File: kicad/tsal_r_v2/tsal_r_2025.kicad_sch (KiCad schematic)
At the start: 46 parts, among them J1 Conn_01x02_Pin, J2 Conn_01x02_Pin, U1 TL431LP, U2 LTV-817, U3 B1212, U4 2N7002, U5 2N7002, U6 NCE60P04R

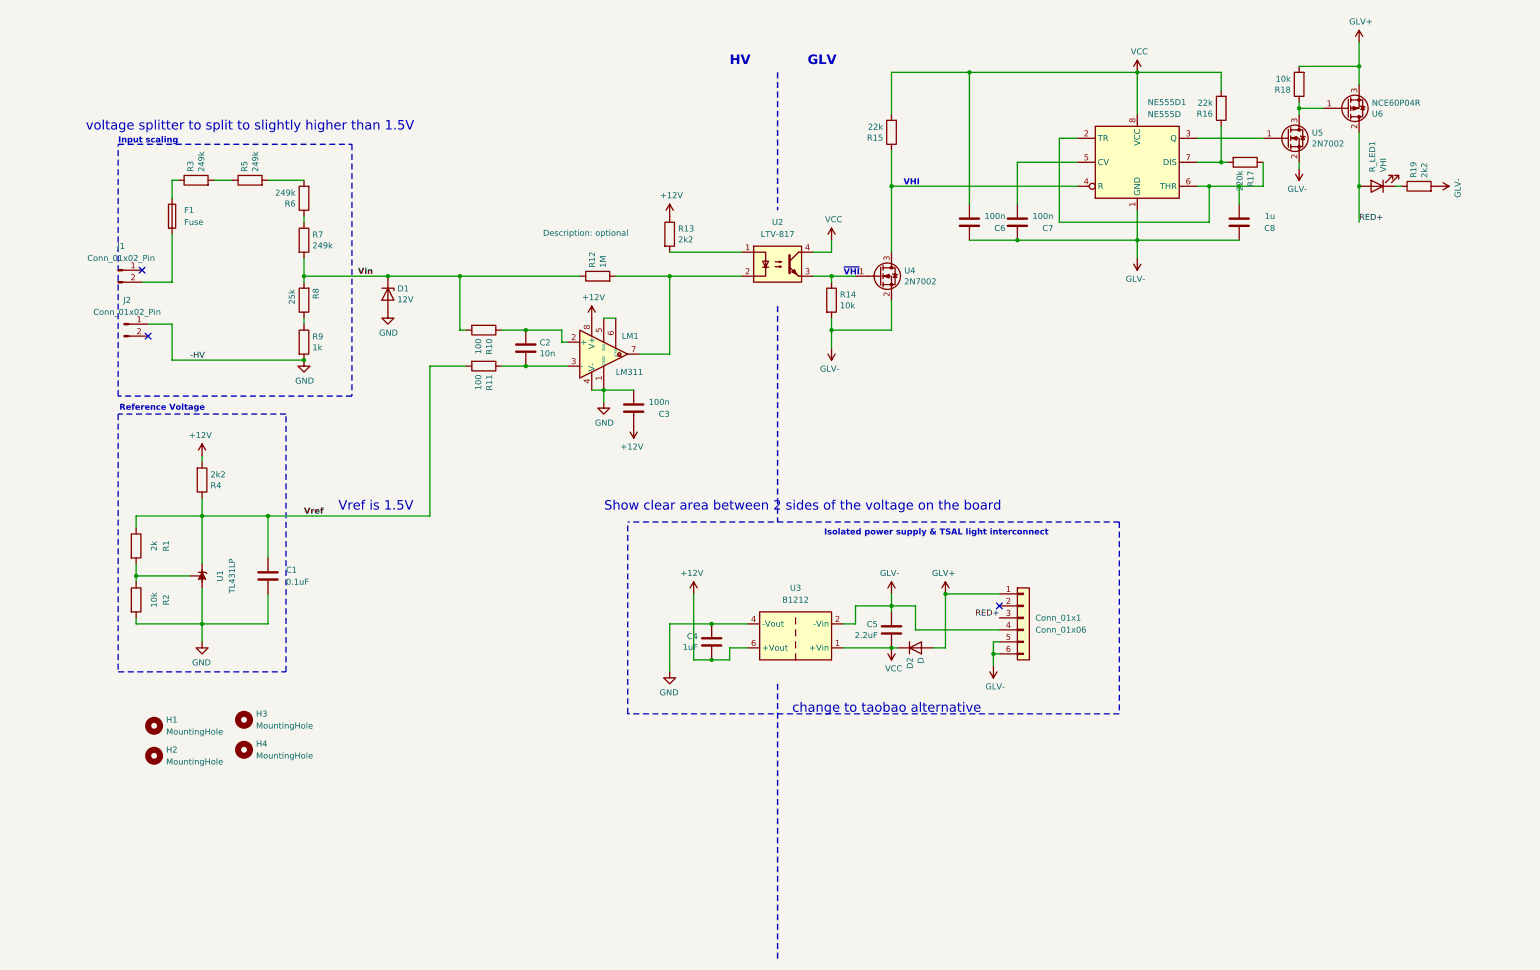
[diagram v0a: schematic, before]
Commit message: TSAL-R v3.0
Redesigned the TSAL-R, currently v3. with naming RBR-TSAL-R v3.0
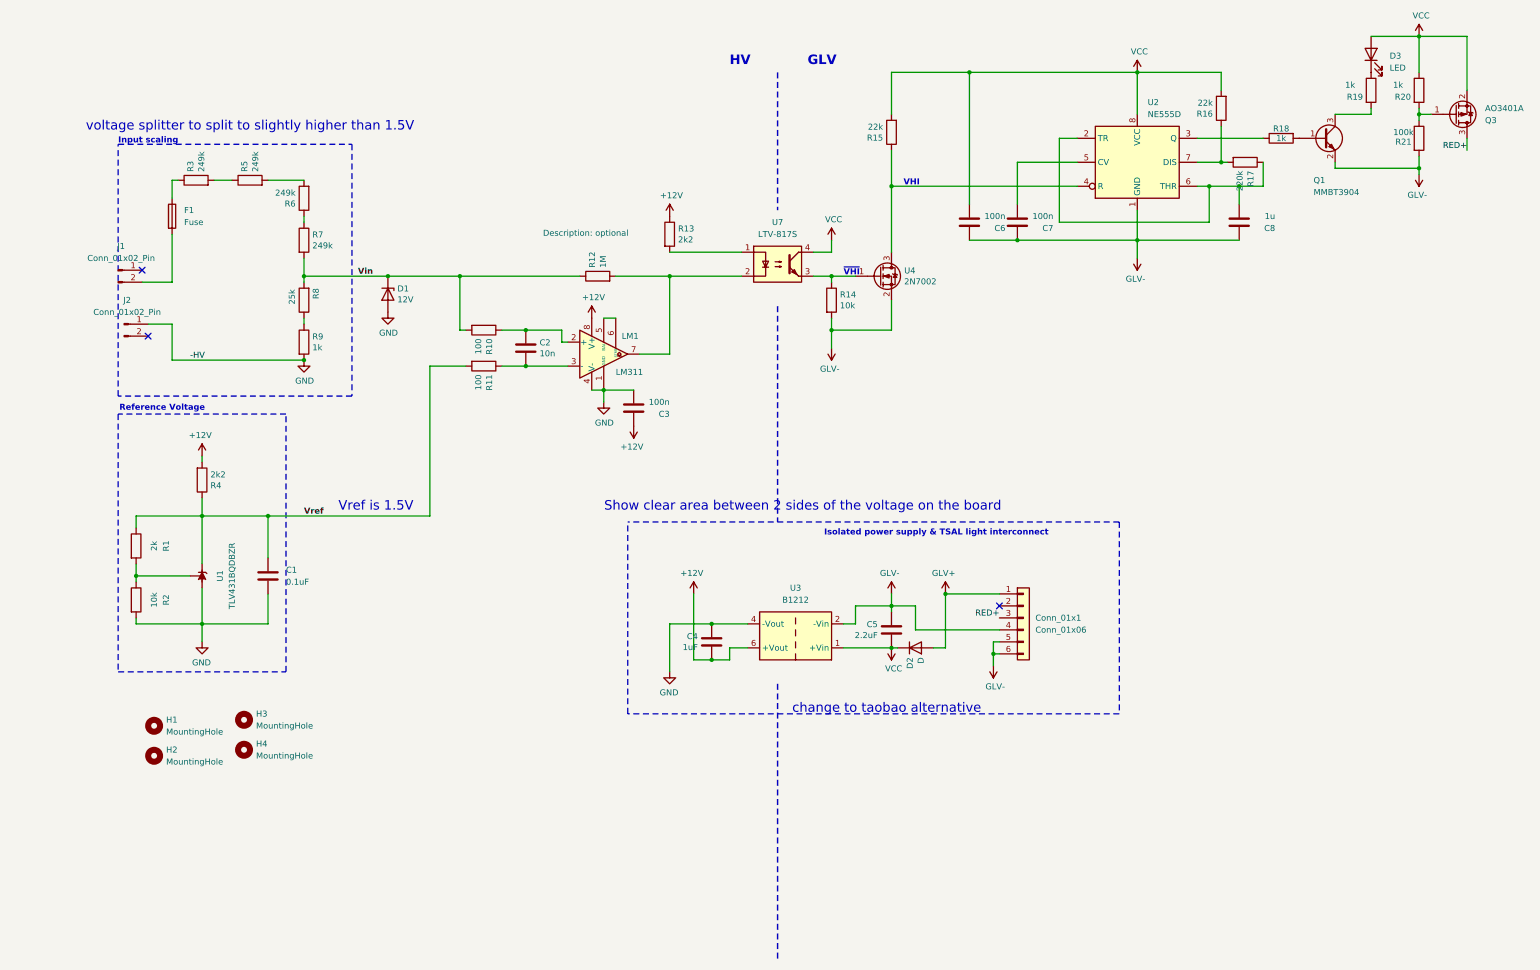
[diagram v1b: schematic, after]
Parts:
- removed R_LED1: VHI, LED_SMD:LED_0805_2012Metric_Pad1.15x1.40mm_HandSolder, symbol Device:LED
- removed U2: LTV-817, Package_DIP:DIP-4_W7.62mm, symbol Isolator:LTV-817
- removed U5: 2N7002, Package_TO_SOT_SMD:SOT-23_Handsoldering, symbol Transistor_FET:2N7002
- removed U6: NCE60P04R, Package_TO_SOT_SMD:SOT-223-3_TabPin2, symbol Device:Q_PMOS_GDS
- added D3: LED, LED_SMD:LED_0805_2012Metric_Pad1.15x1.40mm_HandSolder, symbol Device:LED
- added Q1: MMBT3904, Package_TO_SOT_SMD:SOT-23_Handsoldering, symbol Transistor_BJT:MMBT3904
- added Q3: AO3401A, Package_TO_SOT_SMD:SOT-23_Handsoldering, symbol Transistor_FET:AO3401A
- added R20: 1k, Resistor_SMD:R_0805_2012Metric_Pad1.20x1.40mm_HandSolder, symbol Device:R
- added R21: 100k, Resistor_SMD:R_0805_2012Metric_Pad1.20x1.40mm_HandSolder, symbol Device:R
- added U7: LTV-817S, Package_DIP:SMDIP-4_W9.53mm, symbol Isolator:LTV-817S
- F1: footprint Fuse:Fuse_1210_3225Metric -> Fuse:Fuse_0805_2012Metric_Pad1.15x1.40mm_HandSolder
- R10, R11, R12, R13, R14, R15, R16, R17, R3, R4, R5, R6, R7, R8, R9: footprint Resistor_SMD:R_1206_3216Metric_Pad1.30x1.75mm_HandSolder -> Resistor_SMD:R_0805_2012Metric_Pad1.20x1.40mm_HandSolder
- R18: value 10k -> 1k; footprint Resistor_SMD:R_1206_3216Metric_Pad1.30x1.75mm_HandSolder -> Resistor_SMD:R_0805_2012Metric_Pad1.20x1.40mm_HandSolder
- R19: value 2k2 -> 1k; footprint Resistor_SMD:R_1206_3216Metric_Pad1.30x1.75mm_HandSolder -> Resistor_SMD:R_0805_2012Metric_Pad1.20x1.40mm_HandSolder
- U1: value TL431LP -> TLV431BQDBZR; footprint Package_TO_SOT_THT:TO-92_Inline -> Package_TO_SOT_SMD:SOT-23
- renumbered NE555D1 to U2
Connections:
- net GLV+: no longer R18.2
- net GLV-: now also Q1.2 (E), R21.2; no longer R19.2
- net RED+: now also Q3.3 (D)
- net VCC: now also D3.2 (A), Q3.2 (S), R20.1, U7.4
- net at R19.1: now also D3.1 (K)
- net at LM1.7, R12.2: now also U7.2
- net at R13.2: now also U7.1
- net at R14.1, U4.1 (G): now also U7.3
- net at U2.3 (Q): now also R18.1
- new net: Q1.3 (C), R19.2
- new net: Q3.1 (G), R20.2, R21.1
- new net: Q1.1 (B), R18.2
